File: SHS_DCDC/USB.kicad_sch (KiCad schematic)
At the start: 24 parts, among them J2 USB_A, Q8 Q_PMOS_DGS, U4 LMV358IDR, U5 MP3414A

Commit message: Ubuntu transfer
Commit before transfer onto Ubuntu
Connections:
- net USB_D+: now reaches J2.3 (D+)
- net USB_D+: no longer J2.2 (D-)
- new net USB_D-: J2.2 (D-)
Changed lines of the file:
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@@
-    (stroke (width 0) (type default) (color 0 0 0 0))
-  )
-  (wire (pts (xy 236.22 67.31) (xy 236.22 64.77))
     (stroke (width 0) (type default) (color 0 0 0 0))
   )
@@
     )
   )
+  (global_label "USB_D+" (shape input) (at 236.22 67.31 180) (fields_autoplaced)
+    (effects (font (size 1.27 1.27)) (justify right))
+    (property "Intersheet References" "${INTERSHEET_REFS}" (id 0) (at 226.2758 67.2306 0)
+      (effects (font (size 1.27 1.27)) (justify right) hide)
+    )
+  )
   (global_label "ILIM_USB" (shape input) (at 80.01 102.87 270) (fields_autoplaced)
     (effects (font (size 1.27 1.27)) (justify right))
@@
     )
   )
+  (global_label "USB_D-" (shape input) (at 236.22 64.77 180) (fields_autoplaced)
+    (effects (font (size 1.27 1.27)) (justify right))
+    (property "Intersheet References" "${INTERSHEET_REFS}" (id 0) (at 226.2758 64.6906 0)
+      (effects (font (size 1.27 1.27)) (justify right) hide)
+    )
+  )

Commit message: Commit_190223
Normal commit
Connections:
- net USB_IN renamed LOAD
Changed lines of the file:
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@@
     )
   )
-  (global_label "USB_IN" (shape input) (at 27.94 72.39 180) (fields_autoplaced)
+  (global_label "LOAD" (shape input) (at 27.94 72.39 180) (fields_autoplaced)
     (effects (font (size 1.27 1.27)) (justify right))
-    (property "Intersheet References" "${INTERSHEET_REFS}" (id 0) (at 0 0 0)
-      (effects (font (size 1.27 1.27)) hide)
+    (property "Intersheet References" "${INTERSHEET_REFS}" (id 0) (at 20.8987 72.3106 0)
+      (effects (font (size 1.27 1.27)) (justify right) hide)
     )
   )
@@
     (pin "4")
     (pin "8")
-    (pin "4")
-    (pin "5")
-    (pin "6")
-    (pin "7")
-    (pin "8")
   )
   (symbol (lib_id "SHS_DCDC:LMV358IDR-dk_Linear-Amplifiers-Instrumentation-OP-Amps-Buffer-Amps") (at 213.36 102.87 270) (unit 2)
@@
       (effects (font (size 1.524 1.524)) (justify left) hide)
     )
-    (pin "1")
-    (pin "2")
-    (pin "3")
-    (pin "4")
-    (pin "8")
     (pin "4")
     (pin "5")

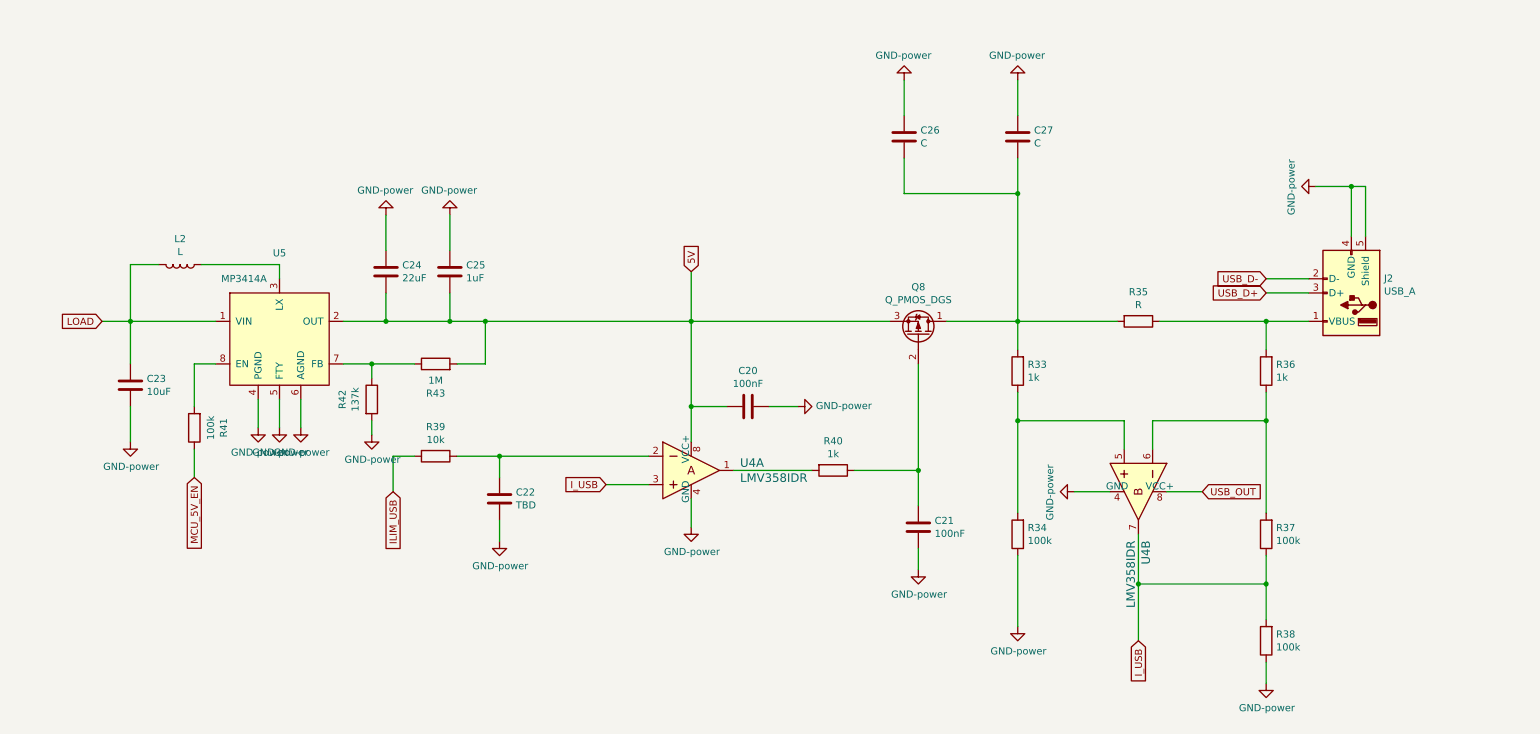
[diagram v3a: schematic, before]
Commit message: Commit010323
Progress on the USB current limitation
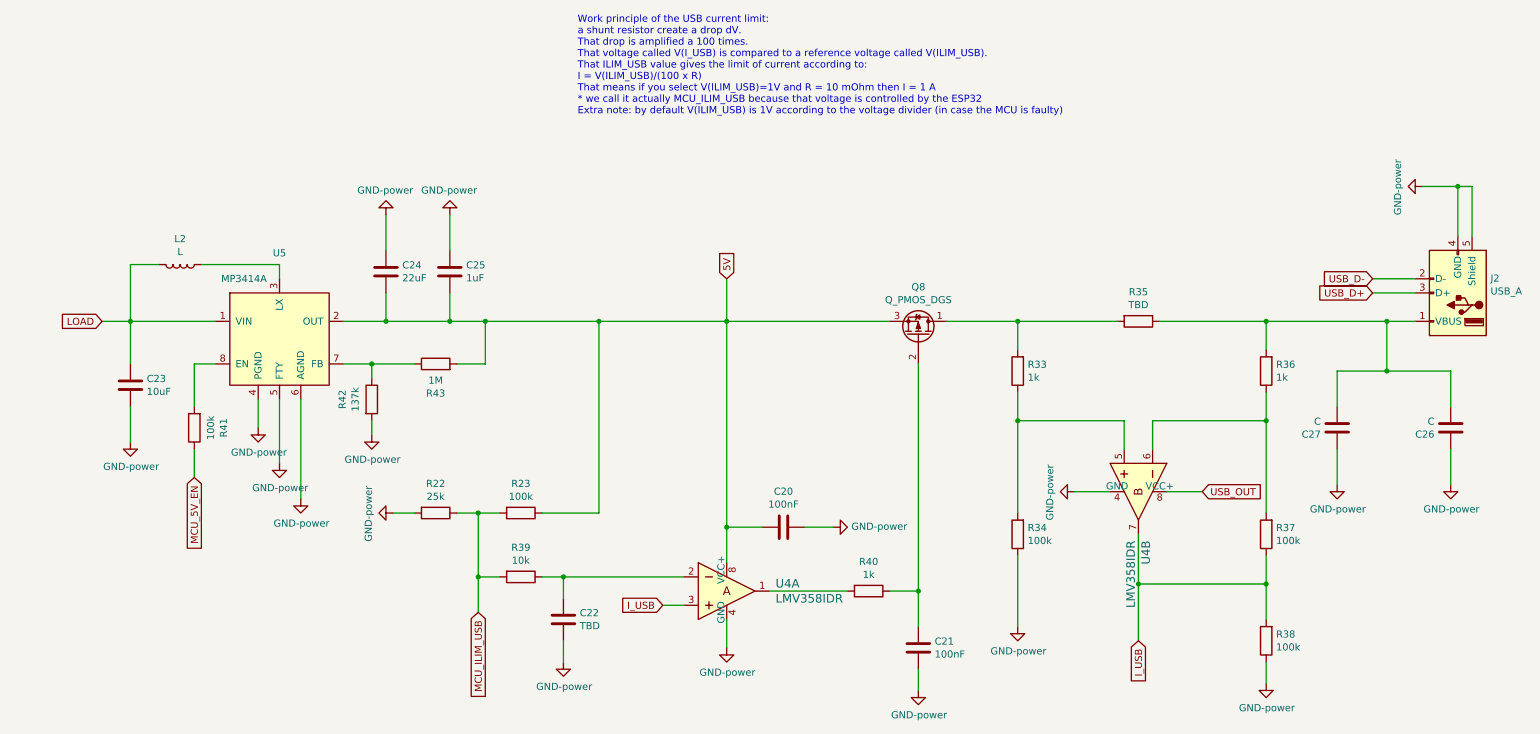
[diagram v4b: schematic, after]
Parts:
- added R22: 25k, Resistor_SMD:R_0603_1608Metric, symbol SHS_DCDC:R-Device
- added R23: 100k, Resistor_SMD:R_0603_1608Metric, symbol SHS_DCDC:R-Device
- R35: value R -> TBD
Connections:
- net 5V: now also R23.1
- net GND: now also R22.2
- net at Q8.1 (D), R33.2, R35.2: no longer C26.2, C27.2
- net at J2.1 (VBUS), R35.1, R36.2: now also C26.2, C27.2
- net ILIM_USB renamed MCU_ILIM_USB
- net MCU_ILIM_USB: now also R22.1, R23.2
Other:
- note added: "Work principle of the USB current limit: a shunt resistor create a drop dV. That drop is amplified a 100 times. That voltage called V(I_USB) is compared to a reference voltage called V(ILIM_USB). That ILIM_USB value gives the limit of current according to: I = V(ILIM_USB)/(100 x R) That means if you select V(ILIM_USB)=1V and R = 10 mOhm then I = 1 A * we call it actually MCU_ILIM_USB because that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"
- moved on the sheet: C20, C21, C22, C26, C27, J2, R39, R40, U4A

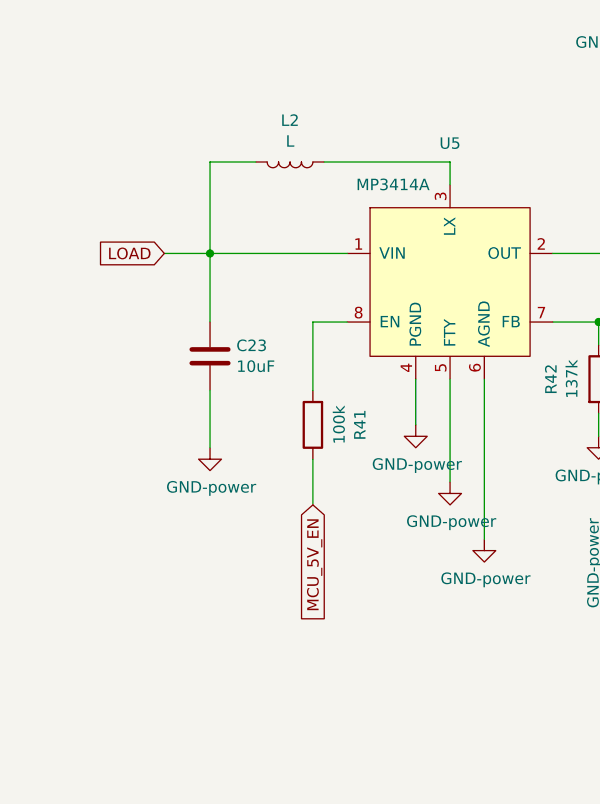
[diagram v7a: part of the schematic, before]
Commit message: 6 layers PCB
Decision to move to a 6 layers PCB to ease the PCB routing
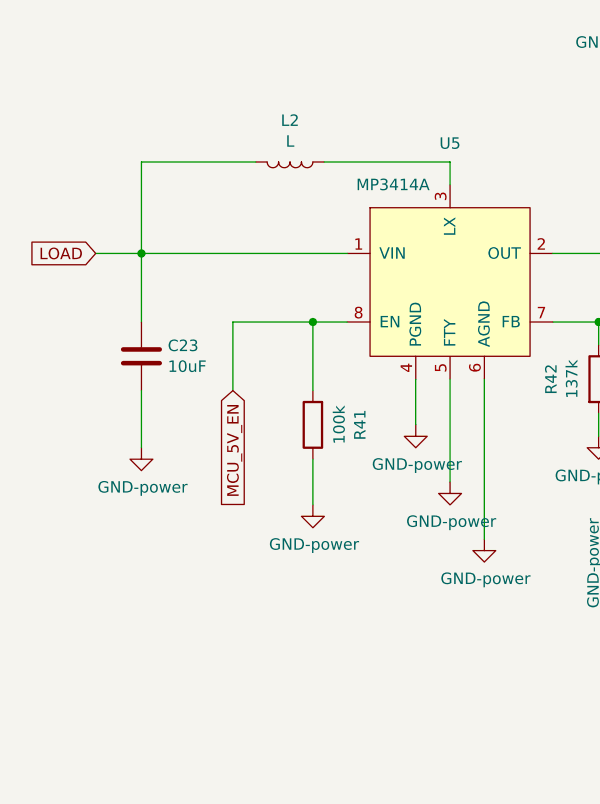
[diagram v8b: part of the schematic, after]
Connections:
- net GND: now also R41.1
- net MCU_5V_EN: now also R41.2, U5.8 (EN); no longer R41.1
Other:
- moved on the sheet: C23
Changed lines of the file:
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@@
   (junction (at 257.81 81.28) (diameter 0) (color 0 0 0 0)
   )
-  (junction (at 33.02 72.39) (diameter 0) (color 0 0 0 0)
+  (junction (at 25.4 72.39) (diameter 0) (color 0 0 0 0)
   )
   (junction (at 191.77 72.39) (diameter 0) (color 0 0 0 0)
@@
   (junction (at 191.77 90.17) (diameter 0) (color 0 0 0 0)
   )
+  (junction (at 44.45 80.01) (diameter 0) (color 0 0 0 0)
+  )
   (junction (at 139.7 72.39) (diameter 0) (color 0 0 0 0)
   )
@@
     (stroke (width 0) (type default) (color 0 0 0 0))
   )
-  (wire (pts (xy 33.02 87.63) (xy 33.02 93.98))
+  (wire (pts (xy 25.4 87.63) (xy 25.4 93.98))
     (stroke (width 0) (type default) (color 0 0 0 0))
   )
@@
     (stroke (width 0) (type default) (color 0 0 0 0))
   )
-  (wire (pts (xy 33.02 72.39) (xy 33.02 80.01))
+  (wire (pts (xy 25.4 72.39) (xy 25.4 80.01))
     (stroke (width 0) (type default) (color 0 0 0 0))
   )
@@
     (stroke (width 0) (type default) (color 0 0 0 0))
   )
+  (wire (pts (xy 35.56 80.01) (xy 44.45 80.01))
+    (stroke (width 0) (type default) (color 0 0 0 0))
+  )
   (wire (pts (xy 191.77 85.09) (xy 191.77 90.17))
     (stroke (width 0) (type default) (color 0 0 0 0))
@@
     (stroke (width 0) (type default) (color 0 0 0 0))
   )
-  (wire (pts (xy 33.02 72.39) (xy 48.26 72.39))
+  (wire (pts (xy 25.4 72.39) (xy 48.26 72.39))
     (stroke (width 0) (type default) (color 0 0 0 0))
   )
@@
     (stroke (width 0) (type default) (color 0 0 0 0))
   )
-  (wire (pts (xy 33.02 72.39) (xy 33.02 62.23))
+  (wire (pts (xy 25.4 72.39) (xy 25.4 62.23))
     (stroke (width 0) (type default) (color 0 0 0 0))
   )
@@
     (stroke (width 0) (type default) (color 0 0 0 0))
   )
-  (wire (pts (xy 33.02 62.23) (xy 38.1 62.23))
+  (wire (pts (xy 25.4 62.23) (xy 38.1 62.23))
     (stroke (width 0) (type default) (color 0 0 0 0))
   )
@@
     (stroke (width 0) (type default) (color 0 0 0 0))
   )
-  (wire (pts (xy 27.94 72.39) (xy 33.02 72.39))
+  (wire (pts (xy 20.32 72.39) (xy 25.4 72.39))
     (stroke (width 0) (type default) (color 0 0 0 0))
   )
   (wire (pts (xy 213.36 119.38) (xy 213.36 129.54))
+    (stroke (width 0) (type default) (color 0 0 0 0))
+  )
+  (wire (pts (xy 35.56 87.63) (xy 35.56 80.01))
     (stroke (width 0) (type default) (color 0 0 0 0))
   )
@@
     )
   )
-  (global_label "MCU_5V_EN" (shape input) (at 44.45 100.33 270) (fields_autoplaced)
+  (global_label "MCU_5V_EN" (shape input) (at 35.56 87.63 270) (fields_autoplaced)
     (effects (font (size 1.27 1.27)) (justify right))
-    (property "Intersheet References" "${INTERSHEET_REFS}" (id 0) (at 0 0 0)
+    (property "Intersheet References" "${INTERSHEET_REFS}" (id 0) (at -8.89 -12.7 0)
       (effects (font (size 1.27 1.27)) hide)
     )
@@
     )
   )
-  (global_label "LOAD" (shape input) (at 27.94 72.39 180) (fields_autoplaced)
+  (global_label "LOAD" (shape input) (at 20.32 72.39 180) (fields_autoplaced)
     (effects (font (size 1.27 1.27)) (justify right))
-    (property "Intersheet References" "${INTERSHEET_REFS}" (id 0) (at 20.8987 72.3106 0)
+    (property "Intersheet References" "${INTERSHEET_REFS}" (id 0) (at 13.2787 72.3106 0)
       (effects (font (size 1.27 1.27)) (justify right) hide)
     )
@@
     (pin "8")
   )
-  (symbol (lib_id "SHS_DCDC:C-Device") (at 33.02 83.82 0) (unit 1)
-    (in_bom yes) (on_board yes)
-    (property "Reference" "C23" (id 0) (at 35.941 82.6516 0)
+  (symbol (lib_id "SHS_DCDC:C-Device") (at 25.4 83.82 0) (unit 1)
+    (in_bom yes) (on_board yes)
+    (property "Reference" "C23" (id 0) (at 28.321 82.6516 0)
       (effects (font (size 1.27 1.27)) (justify left))
     )
-    (property "Value" "10uF" (id 1) (at 35.941 84.963 0)
+    (property "Value" "10uF" (id 1) (at 28.321 84.963 0)
       (effects (font (size 1.27 1.27)) (justify left))
     )
-    (property "Footprint" "Capacitor_SMD:C_0805_2012Metric" (id 2) (at 33.9852 87.63 0)
-      (effects (font (size 1.27 1.27)) hide)
-    )
-    (property "Datasheet" "~" (id 3) (at 33.02 83.82 0)
-      (effects (font (size 1.27 1.27)) hide)
-    )
-    (pin "1")
-    (pin "2")
-  )
-  (symbol (lib_id "SHS_DCDC:GND-power") (at 33.02 93.98 0) (unit 1)
-    (in_bom yes) (on_board yes)
-    (property "Reference" "#PWR043" (id 0) (at 33.02 100.33 0)
-      (effects (font (size 1.27 1.27)) hide)
-    )
-    (property "Value" "GND-power" (id 1) (at 33.147 98.3742 0))
-    (property "Footprint" "" (id 2) (at 33.02 93.98 0)
-      (effects (font (size 1.27 1.27)) hide)
-    )
-    (property "Datasheet" "" (id 3) (at 33.02 93.98 0)
+    (property "Footprint" "Capacitor_SMD:C_0805_2012Metric" (id 2) (at 26.3652 87.63 0)
+      (effects (font (size 1.27 1.27)) hide)
+    )
+    (property "Datasheet" "~" (id 3) (at 25.4 83.82 0)
+      (effects (font (size 1.27 1.27)) hide)
+    )
+    (pin "1")
+    (pin "2")
+  )
+  (symbol (lib_id "SHS_DCDC:GND-power") (at 25.4 93.98 0) (unit 1)
+    (in_bom yes) (on_board yes)
+    (property "Reference" "#PWR043" (id 0) (at 25.4 100.33 0)
+      (effects (font (size 1.27 1.27)) hide)
+    )
+    (property "Value" "GND-power" (id 1) (at 25.527 98.3742 0))
+    (property "Footprint" "" (id 2) (at 25.4 93.98 0)
+      (effects (font (size 1.27 1.27)) hide)
+    )
+    (property "Datasheet" "" (id 3) (at 25.4 93.98 0)
       (effects (font (size 1.27 1.27)) hide)
     )
@@
     (pin "2")
   )
+  (symbol (lib_id "SHS_DCDC:GND-power") (at 44.45 100.33 0) (unit 1)
+    (in_bom yes) (on_board yes)
+    (property "Reference" "#PWR0125" (id 0) (at 44.45 106.68 0)
+      (effects (font (size 1.27 1.27)) hide)
+    )
+    (property "Value" "GND-power" (id 1) (at 44.577 104.7242 0))
+    (property "Footprint" "" (id 2) (at 44.45 100.33 0)
+      (effects (font (size 1.27 1.27)) hide)
+    )
+    (property "Datasheet" "" (id 3) (at 44.45 100.33 0)
+      (effects (font (size 1.27 1.27)) hide)
+    )
+    (pin "1")
+  )
   (symbol (lib_id "SHS_DCDC:R-Device") (at 87.63 106.68 270) (unit 1)
